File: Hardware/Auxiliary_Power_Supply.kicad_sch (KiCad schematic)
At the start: 24 parts, among them U7 TLV1117-33, U9 LV14340DDAR

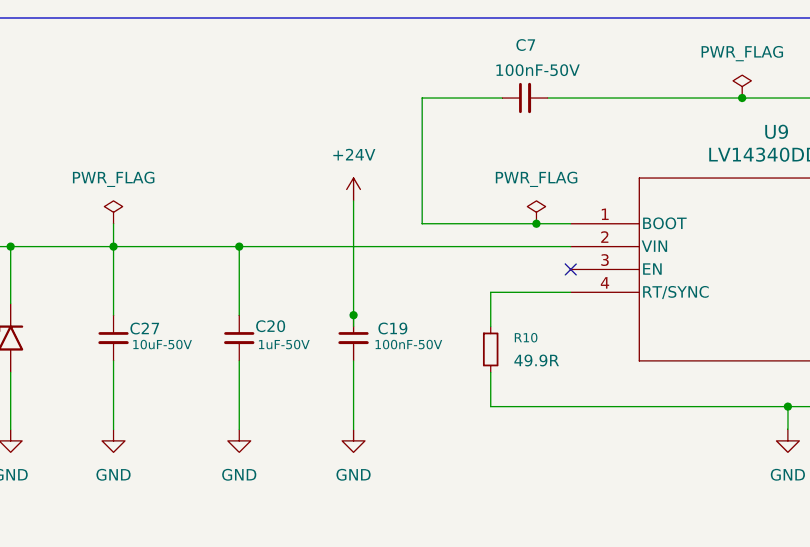
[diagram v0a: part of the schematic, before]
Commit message: fix(hardware): reroute PCB for schematic updates
Synchronize PCB routing and net assignments with the revised optocoupler control design, including related auxiliary power and USB signal wiring updates.
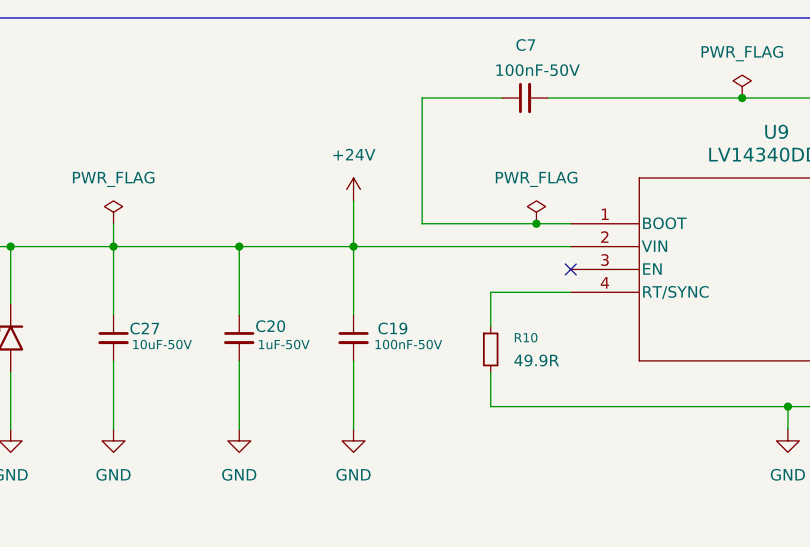
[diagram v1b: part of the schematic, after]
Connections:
- net +24V: now also C20.1, C27.1, D4.1 (A1), F3.2, U9.2 (VIN)
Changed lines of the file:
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@@
+	)
+	(junction
+		(at 109.22 58.42)
+		(diameter 0)
+		(color 0 0 0 0)
 	)
 	(junction
 		(at 224.79 41.91)
-		(diameter 0)
-		(color 0 0 0 0)
-	)
-	(junction
-		(at 109.22 66.04)
 		(diameter 0)
 		(color 0 0 0 0)
@@
 	(wire
 		(pts
+			(xy 109.22 58.42) (xy 133.35 58.42)
+		)
+		(stroke
+			(width 0)
+			(type default)
+		)
+	)
+	(wire
+		(pts
+			(xy 109.22 53.34) (xy 109.22 58.42)
+		)
+		(stroke
+			(width 0)
+			(type default)
+		)
+	)
+	(wire
+		(pts
 			(xy 109.22 114.3) (xy 107.95 114.3)
 		)
@@
 	(wire
 		(pts
-			(xy 109.22 53.34) (xy 109.22 66.04)
-		)
-		(stroke
-			(width 0)
-			(type default)
-		)
-	)
-	(wire
-		(pts
 			(xy 82.55 71.12) (xy 82.55 78.74)
 		)
@@
 	(wire
 		(pts
+			(xy 109.22 58.42) (xy 109.22 66.04)
+		)
+		(stroke
+			(width 0)
+			(type default)
+		)
+	)
+	(wire
+		(pts
 			(xy 116.84 41.91) (xy 125.73 41.91)
 		)
@@
 	(wire
 		(pts
-			(xy 109.22 67.31) (xy 109.22 66.04)
-		)
-		(stroke
-			(width 0)
-			(type default)
-		)
-	)
-	(wire
-		(pts
 			(xy 74.93 114.3) (xy 74.93 111.76)
 		)
@@
 	(wire
 		(pts
-			(xy 96.52 58.42) (xy 133.35 58.42)
-		)
-		(stroke
+			(xy 96.52 58.42) (xy 109.22 58.42)
+		)
+		(stroke
